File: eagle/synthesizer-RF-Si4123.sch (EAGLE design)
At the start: 34 parts, among them U2 SI4123, X1 SMA-142-0701-801/806, X2 SMA-142-0701-801/806, X23 ECS-TXO-3225, X3 SMA-142-0701-801/806

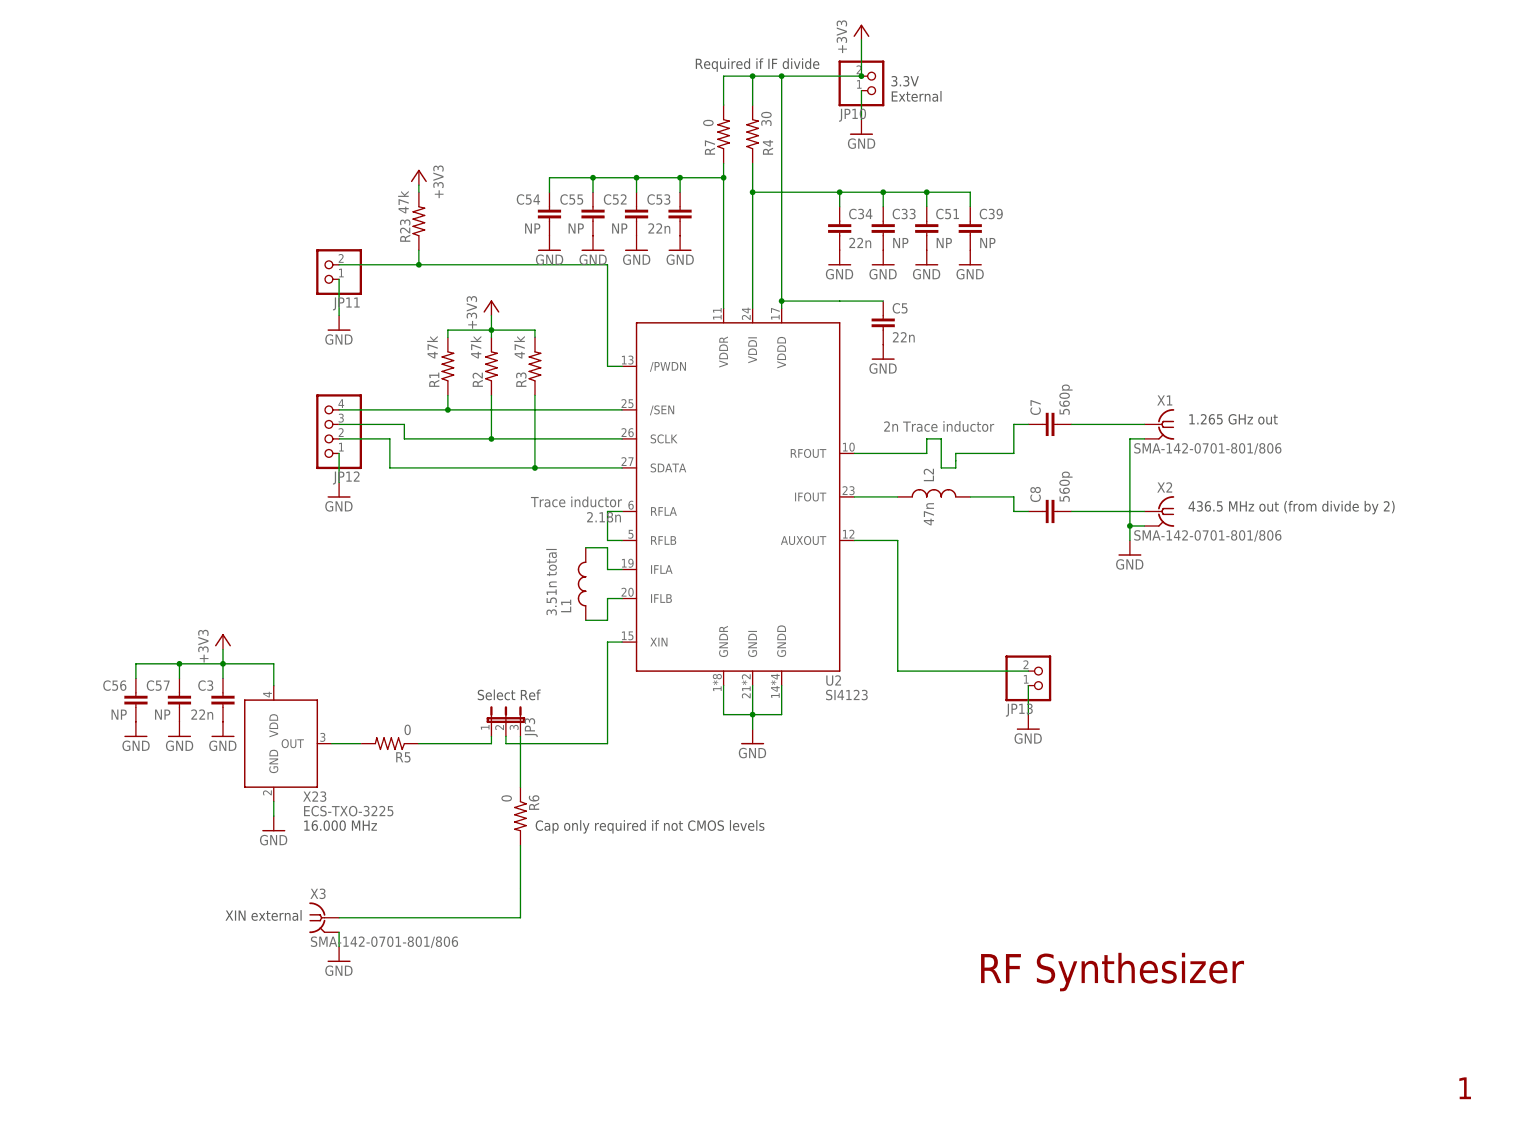
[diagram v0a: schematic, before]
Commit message: Revise passives, add TCXO options
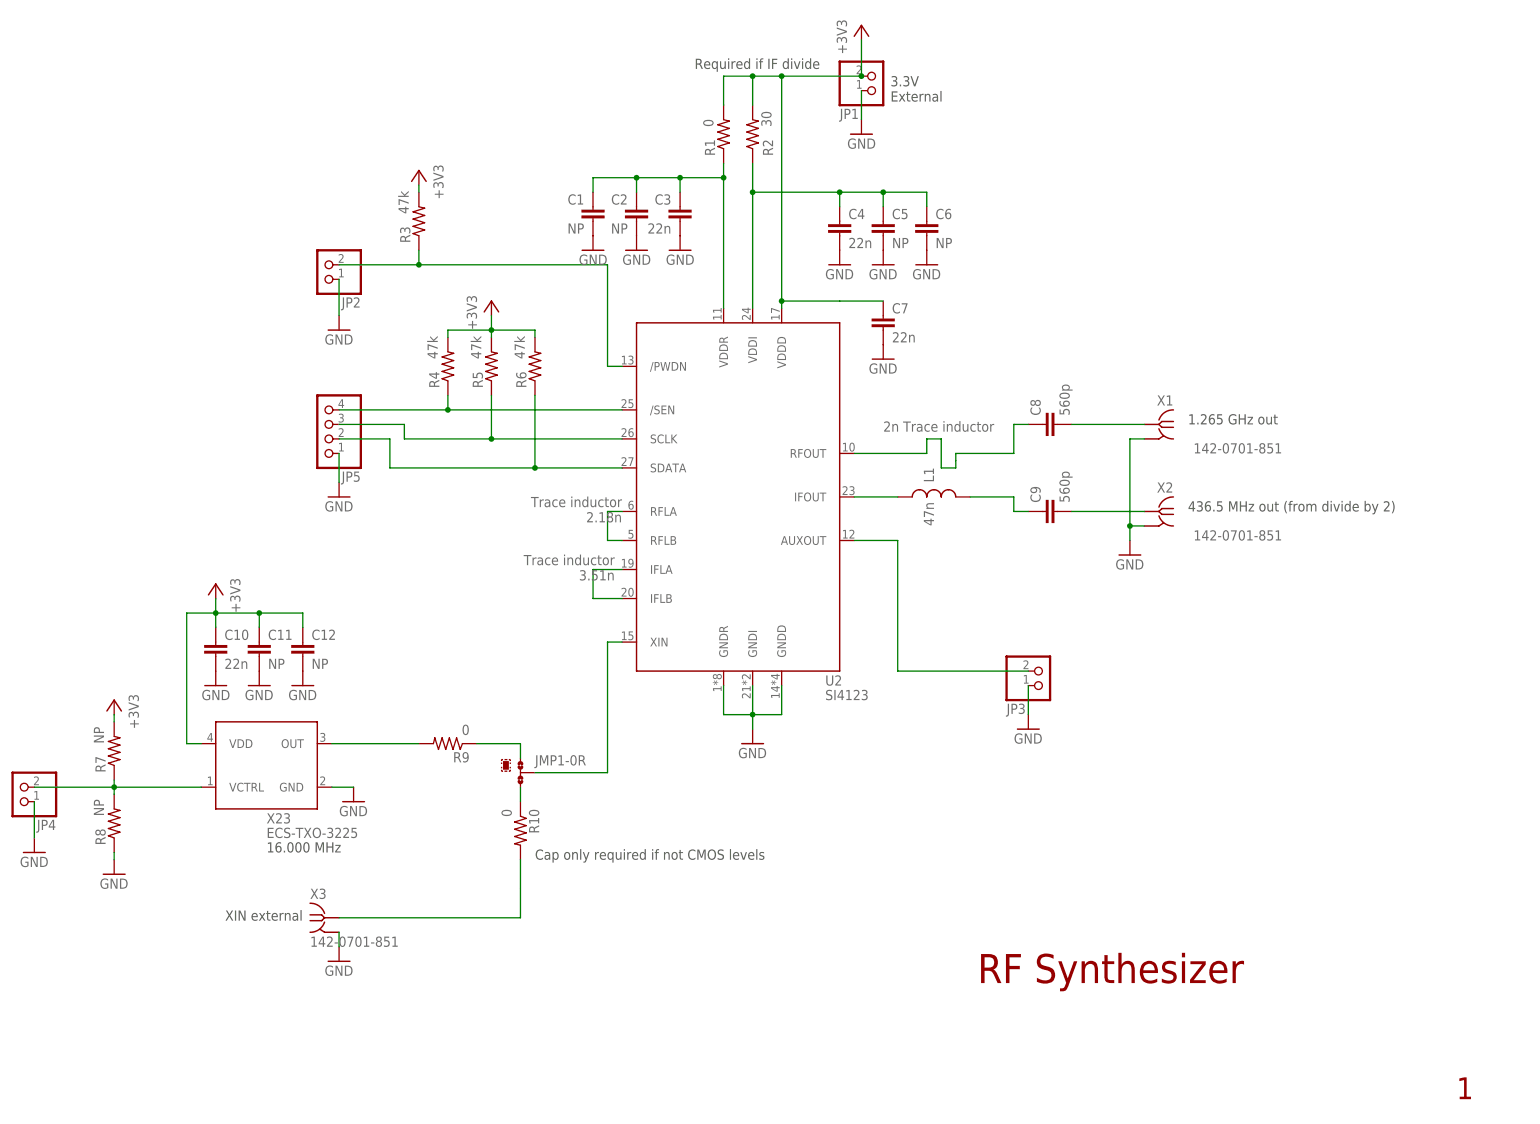
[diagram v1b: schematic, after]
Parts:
- removed C33, C39, C54, C56, C57: NP, oresat-rcl:C-EU0603-B-NOSILK
- removed C53: 22n, oresat-rcl:C-EU0603-B-NOSILK
- removed JP13: (no value), pinhead:PINHD-1X2
- removed L2: 47n, oresat-rcl:L-US0201-B-NOSILK
- removed R23: 47k, oresat-rcl:R-US_0402-B-NOSILK
- added C10: 22n, oresat-rcl:C-EU0603-B-NOSILK
- added C11, C12: NP, oresat-rcl:C-EU0603-B-NOSILK
- added C9: 560p, oresat-rcl:C-EU0402-B-NOSILK
- added JMP1: 0R-JUMPA, jump-0r-smd:0R-JUMPA
- added JP4: (no value), pinhead:PINHD-1X2
- added R10, R9: 0, oresat-rcl:R-US_0402-B-NOSILK
- added R8: NP, oresat-rcl:R-US_0805-B-NOSILK
- C5: value 22n -> NP
- C7: value 560p -> 22n; device oresat-rcl:C-EU0402-B-NOSILK -> oresat-rcl:C-EU0603-B-NOSILK
- JP3: device jumper:JP2E -> pinhead:PINHD-1X2
- L1: value 3.51n total -> 47n; device oresat-rcl:L-US0201-B-NOSILK -> oresat-rcl:L-US0402-B-NOSILK
- R1: value 47k -> 0; device oresat-rcl:R-US_0402-B-NOSILK -> oresat-rcl:R-US_0805-B-NOSILK
- R2: value 47k -> 30; device oresat-rcl:R-US_0402-B-NOSILK -> oresat-rcl:R-US_0805-B-NOSILK
- R4: value 30 -> 47k; device oresat-rcl:R-US_0805-B-NOSILK -> oresat-rcl:R-US_0402-B-NOSILK
- R5, R6: value 0 -> 47k
- R7: value 0 -> NP
- X1, X2, X3: value SMA-142-0701-801/806 -> 142-0701-851; device con-coax:SMA-142-0701-801/806 -> J-Cinch-142-0701-851-SMA-end-launch:142-0701-851
- renumbered C34 to C4, C51 to C6, C52 to C2, C55 to C1, JP10 to JP1, JP11 to JP2, JP12 to JP5
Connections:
- removed net N$12: L1.2, U2.IFLB
- removed net N$21: JP3.3, R6.1
- new net N$17: JMP1-0R.2, U2.XIN
- new net N$19: JP4.2, R7.1, R8.2, X23.VCTRL
- net +3V3: now also C10.1, C11.1, C12.1, C7.1, R5.2, R6.2; no longer C3.1, C5.1, C56.1, C57.1, R23.2
- net GND: now also C10.2, C11.2, C12.2, C7.2, JP3.1, JP4.1, R8.1, X1.GND, X2.GND, X3.GND; no longer C33.2, C39.2, C53.2, C54.2, C56.2, C57.2, JP13.1, X1.2, X2.2, X3.2
- net N$1: now also JMP1-0R.3, R10.1; no longer JP3.2, U2.XIN
- net N$10: now also R10.2, X3.RF; no longer R6.2, X3.1
- net N$11: now also C9.1, L1.2; no longer C8.1, L2.2
- net N$13: now also L1.1; no longer L2.1
- net N$14: now also C8.1; no longer C7.1
- net N$15: now also C3.1, R1.1; no longer C53.1, C54.1, R7.1
- net N$16: now also C8.2, X1.RF; no longer C7.2, X1.1
- net N$18: now also C9.2, X2.RF; no longer C8.2, X2.1
- net N$20: now also R9.2; no longer R5.2
- net N$3: now also U2.IFLB; no longer L1.1
- net N$4: now also R3.1; no longer R23.1
- net N$5: now also R4.1; no longer R1.1
- net N$6: now also R5.1; no longer R2.1
- net N$7: now also R6.1; no longer R3.1
- net N$8: now also JP3.2; no longer JP13.2
- net N$9: now also JMP1-0R.1, R9.1; no longer JP3.1, R5.1
- net N$93: now also C5.1, R2.1; no longer C33.1, C39.1, R4.1
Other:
- note added: "Trace inductor 3.51n"
- note removed: "Select Ref"
- moved on the sheet: C3, C5, C7, C8, L1, R1, R2, R3, R4, R5, R6, R7

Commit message: Add LDO, LED on auxout
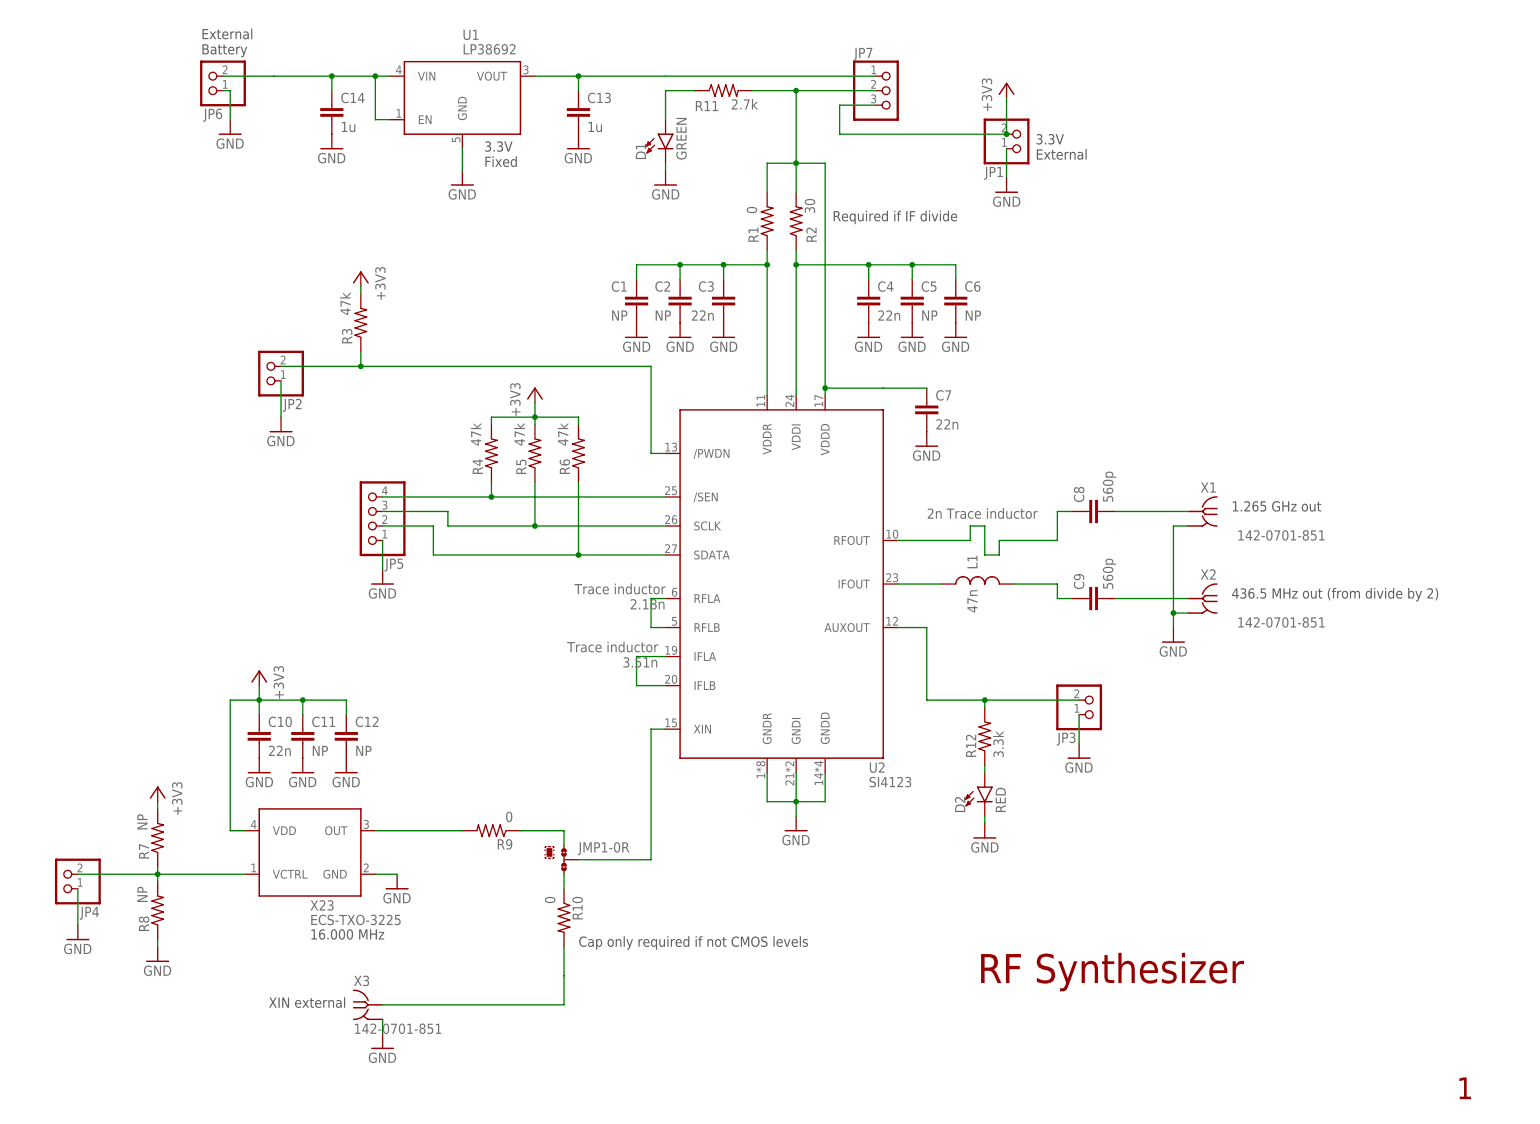
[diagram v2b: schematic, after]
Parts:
- added C13, C14: 1u, oresat-rcl:C-EU0603-B-NOSILK
- added D1: GREEN, SparkFun-LED:LED-GREEN0603
- added D2: RED, SparkFun-LED:LED-GREEN0603
- added JP6: (no value), pinhead:PINHD-1X2
- added JP7: (no value), pinhead:PINHD-1X3
- added R11: 2.7k, oresat-rcl:R-US_0603-B-NOSILK
- added R12: 3.3k, oresat-rcl:R-US_0603-B-NOSILK
- added U1: LP38692, U-TI-LP38692-linear-reg:LP38692
- R7, R8: device oresat-rcl:R-US_0805-B-NOSILK -> oresat-rcl:R-US_0603-B-NOSILK
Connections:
- new net N$12: C7.1, JP7.2, R1.2, R11.2, R2.2, U2.VDDD
- new net N$21: D1.A, R11.1
- new net N$22: D2.A, R12.1
- new net N$77: C14.1, JP6.2, U1.EN, U1.VIN
- new net N$89: C13.1, JP7.1, U1.VOUT
- net +3V3: now also JP7.3; no longer C7.1, R1.2, R2.2, U2.VDDD
- net GND: now also C13.2, C14.2, D1.C, D2.C, JP6.1, U1.GND
- net N$8: now also R12.2
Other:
- note added: "3.3V Fixed"
- note added: "External Battery"
- moved on the sheet: C1, C10, C11, C12, C2, C3, C4, C5, C6, C7, C8, C9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

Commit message: Add synthesizer-RF-Si4123.brd
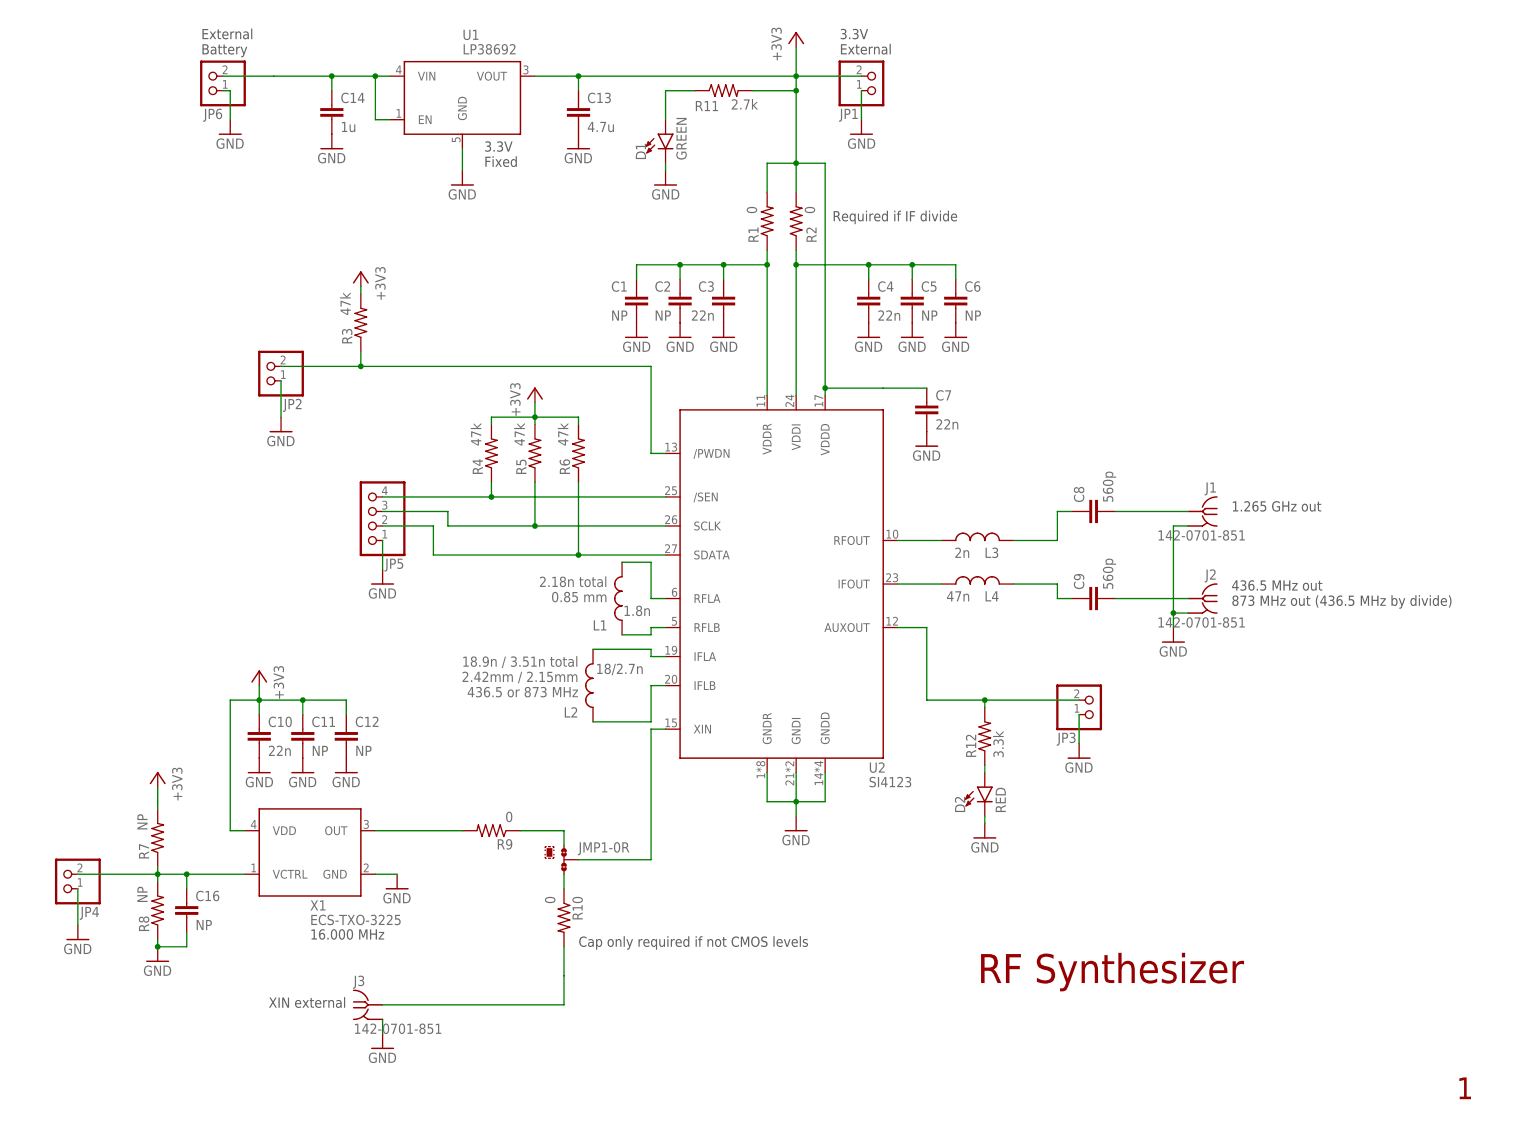
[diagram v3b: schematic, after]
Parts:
- removed JP7: (no value), pinhead:PINHD-1X3
- removed X23: ECS-TXO-3225, X-ECS-TXO-TCXO:ECS-TXO-3225
- added C16: NP, oresat-rcl:C-EU0603-B-NOSILK
- added J1: 142-0701-851, J-Cinch-142-0701-851-SMA-end-launch:142-0701-851
- added L2: 18/2.7n, oresat-rcl:L-US0402-C-NOSILK
- added L3: 2n, oresat-rcl:L-US0402-B-NOSILK
- added L4: 47n, oresat-rcl:L-US0402-B-NOSILK
- C13: value 1u -> 4.7u; device oresat-rcl:C-EU0603-B-NOSILK -> oresat-rcl:C-EU0805-B-NOSILK
- L1: value 47n -> 1.8n; device oresat-rcl:L-US0402-B-NOSILK -> oresat-rcl:L-US0402-C-NOSILK
- R2: value 30 -> 0
- X1: value 142-0701-851 -> ECS-TXO-3225; device J-Cinch-142-0701-851-SMA-end-launch:142-0701-851 -> X-ECS-TXO-TCXO:ECS-TXO-3225
- renumbered X2 to J2, X3 to J3
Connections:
- net N$10 renamed REF_IN
- net N$18 renamed IF_OUT
- net N$77 renamed +BAT
- removed net N$12: C7.1, JP7.2, R1.2, R11.2, R2.2, U2.VDDD
- removed net N$16: C8.2, X1.RF
- removed net N$89: C13.1, JP7.1, U1.VOUT
- new net N$23: L2.2, U2.IFLA
- new net N$24: L2.1, U2.IFLB
- new net N$25: L3.1, U2.RFOUT
- new net RF_OUT: C8.2, J1.RF
- net +3V3: now also C13.1, C7.1, R1.2, R11.2, R2.2, U1.VOUT, U2.VDDD, X1.VDD; no longer JP7.3, X23.VDD
- net GND: now also C16.2, J1.GND; no longer X23.GND
- net N$11: now also L4.2; no longer L1.2
- net N$13: now also L4.1; no longer L1.1
- net N$14: now also L3.2; no longer U2.RFOUT
- net N$19: now also C16.1, X1.VCTRL; no longer X23.VCTRL
- net N$2: now also L1.2; no longer U2.RFLB
- net N$20: now also X1.OUT; no longer X23.OUT
- net N$3: now also L1.1, U2.RFLB; no longer U2.IFLA, U2.IFLB
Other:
- note added: "18.9n / 3.51n total 2.42mm / 2.15mm 436.5 or 873 MHz"
- note added: "2.18n total 0.85 mm"
- note added: "436.5 MHz out 873 MHz out (436.5 MHz by divide)"
- note removed: "2n Trace inductor"
- note removed: "436.5 MHz out (from divide by 2)"
- note removed: "Trace inductor 2.18n"
- note removed: "Trace inductor 3.51n"
- moved on the sheet: JP1, L1
